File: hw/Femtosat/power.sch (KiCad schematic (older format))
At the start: 10 parts, among them U0 AP7215-33YG-13

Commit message: Added library for certain components. Symbols and footprints were associated.
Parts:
- C2a1, C2b1, C3a1, C3b1, C4, C5, Cr1, Cr2: footprint Capacitor_SMD:C_0805_2012Metric_Pad1.15x1.40mm_HandSolder -> Capacitor_SMD:C_0603_1608Metric_Pad1.05x0.95mm_HandSolder
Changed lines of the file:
@@
 F 0 "C2b1" H 5165 3696 50  0000 L CNN
 F 1 "100nF" H 5165 3605 50  0000 L CNN
-F 2 "Capacitor_SMD:C_0805_2012Metric_Pad1.15x1.40mm_HandSolder" H 5088 3500 50  0001 C CNN
+F 2 "Capacitor_SMD:C_0603_1608Metric_Pad1.05x0.95mm_HandSolder" H 5088 3500 50  0001 C CNN
 F 3 "~" H 5050 3650 50  0001 C CNN
 	1    5050 3650
@@
 F 0 "C5" H 5215 4846 50  0000 L CNN
 F 1 "1uF" H 5215 4755 50  0000 L CNN
-F 2 "Capacitor_SMD:C_0805_2012Metric_Pad1.15x1.40mm_HandSolder" H 5138 4650 50  0001 C CNN
+F 2 "Capacitor_SMD:C_0603_1608Metric_Pad1.05x0.95mm_HandSolder" H 5138 4650 50  0001 C CNN
 F 3 "~" H 5100 4800 50  0001 C CNN
 	1    5100 4800
@@
 F 0 "C2a1" H 4715 3696 50  0000 L CNN
 F 1 "10uF" H 4715 3605 50  0000 L CNN
-F 2 "Capacitor_SMD:C_0805_2012Metric_Pad1.15x1.40mm_HandSolder" H 4638 3500 50  0001 C CNN
+F 2 "Capacitor_SMD:C_0603_1608Metric_Pad1.05x0.95mm_HandSolder" H 4638 3500 50  0001 C CNN
 F 3 "~" H 4600 3650 50  0001 C CNN
 	1    4600 3650
@@
 F 0 "C4" H 4265 4846 50  0000 L CNN
 F 1 "10uF" H 4265 4755 50  0000 L CNN
-F 2 "Capacitor_SMD:C_0805_2012Metric_Pad1.15x1.40mm_HandSolder" H 4188 4650 50  0001 C CNN
+F 2 "Capacitor_SMD:C_0603_1608Metric_Pad1.05x0.95mm_HandSolder" H 4188 4650 50  0001 C CNN
 F 3 "~" H 4150 4800 50  0001 C CNN
 	1    4150 4800
@@
 F 0 "C3a1" H 4715 4296 50  0000 L CNN
 F 1 "100nF" H 4715 4205 50  0000 L CNN
-F 2 "Capacitor_SMD:C_0805_2012Metric_Pad1.15x1.40mm_HandSolder" H 4638 4100 50  0001 C CNN
+F 2 "Capacitor_SMD:C_0603_1608Metric_Pad1.05x0.95mm_HandSolder" H 4638 4100 50  0001 C CNN
 F 3 "~" H 4600 4250 50  0001 C CNN
 	1    4600 4250
@@
 F 0 "C3b1" H 5165 4296 50  0000 L CNN
 F 1 "100nF" H 5165 4205 50  0000 L CNN
-F 2 "Capacitor_SMD:C_0805_2012Metric_Pad1.15x1.40mm_HandSolder" H 5088 4100 50  0001 C CNN
+F 2 "Capacitor_SMD:C_0603_1608Metric_Pad1.05x0.95mm_HandSolder" H 5088 4100 50  0001 C CNN
 F 3 "~" H 5050 4250 50  0001 C CNN
 	1    5050 4250
@@
 F 0 "Cr1" H 3115 3646 50  0000 L CNN
 F 1 "1uF" H 3115 3555 50  0000 L CNN
-F 2 "Capacitor_SMD:C_0805_2012Metric_Pad1.15x1.40mm_HandSolder" H 3038 3450 50  0001 C CNN
+F 2 "Capacitor_SMD:C_0603_1608Metric_Pad1.05x0.95mm_HandSolder" H 3038 3450 50  0001 C CNN
 F 3 "~" H 3000 3600 50  0001 C CNN
 	1    3000 3600
@@
 F 0 "Cr2" H 4115 3646 50  0000 L CNN
 F 1 "1uF" H 4115 3555 50  0000 L CNN
-F 2 "Capacitor_SMD:C_0805_2012Metric_Pad1.15x1.40mm_HandSolder" H 4038 3450 50  0001 C CNN
+F 2 "Capacitor_SMD:C_0603_1608Metric_Pad1.05x0.95mm_HandSolder" H 4038 3450 50  0001 C CNN
 F 3 "~" H 4000 3600 50  0001 C CNN
 	1    4000 3600

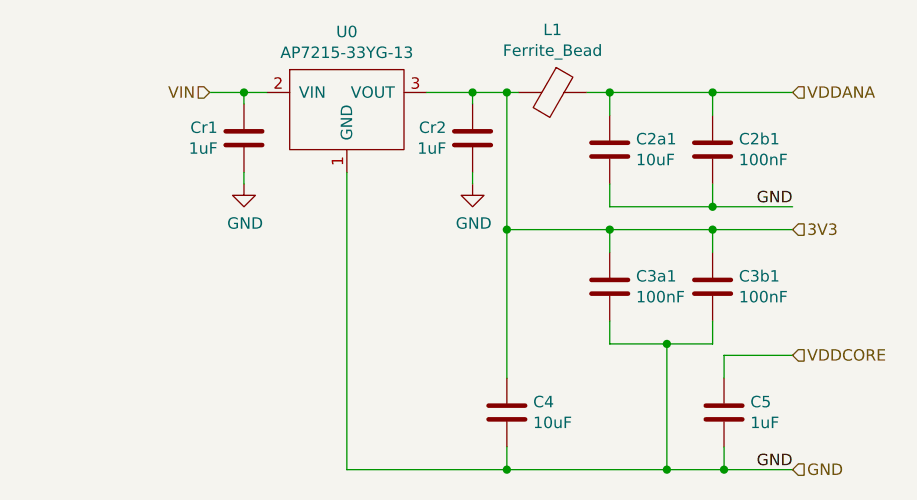
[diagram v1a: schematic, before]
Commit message: Deleted the GPS device (moved to another PCB). Added the deploy-sensor (an interrupter). Moved the programmer to its own hierarchical sheet.
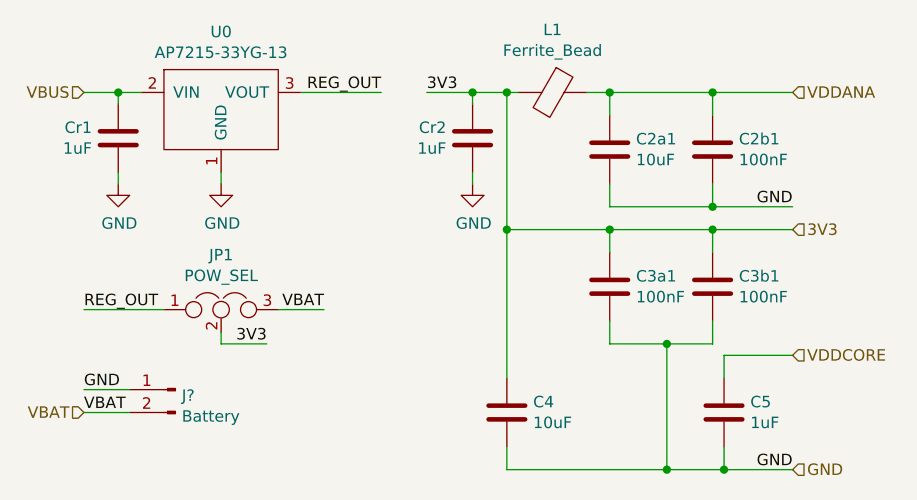
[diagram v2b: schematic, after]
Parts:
- added J?: Battery, symbol Connector:Conn_01x02_Male
- added JP1: POW_SEL, symbol Device:Jumper_NC_Dual
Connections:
- net 3V3: now also JP1.2; no longer U0.3 (VOUT)
- net GND: now also J?.1 (Pin_1)
- net VIN renamed VBUS
- new net REG_OUT: JP1.1, U0.3 (VOUT)
- new net VBAT: J?.2 (Pin_2), JP1.3
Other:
- moved on the sheet: Cr1, U0
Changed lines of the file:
@@
 $Descr A4 11693 8268
 encoding utf-8
-Sheet 2 4
+Sheet 2 5
 Title ""
 Date ""
@@
 L power_regul:AP7215-33YG-13 U0
 U 1 1 5BB07412
-P 3450 3550
-F 0 "U0" H 3450 3965 50  0000 C CNN
-F 1 "AP7215-33YG-13" H 3450 3874 50  0000 C CNN
-F 2 "Package_TO_SOT_SMD:SOT-89-3_Handsoldering" H 3450 3550 50  0001 C CNN
-F 3 "" H 3450 3550 50  0001 C CNN
-	1    3450 3550
+P 2900 3550
+F 0 "U0" H 2900 3965 50  0000 C CNN
+F 1 "AP7215-33YG-13" H 2900 3874 50  0000 C CNN
+F 2 "Package_TO_SOT_SMD:SOT-89-3_Handsoldering" H 2900 3550 50  0001 C CNN
+F 3 "" H 2900 3550 50  0001 C CNN
+	1    2900 3550
 	1    0    0    -1
 $EndComp
@@
 	5400 4000 5050 4000
 Connection ~ 5050 4000
-Connection ~ 4150 5050
-Text HLabel 2850 3400 0    50   Input ~ 0
-VIN
+Text HLabel 2300 3400 0    50   Input ~ 0
+VBUS
 $Comp
 L Device:C Cr1
 U 1 1 5BB30701
-P 3000 3600
-F 0 "Cr1" H 3115 3646 50  0000 L CNN
-F 1 "1uF" H 3115 3555 50  0000 L CNN
-F 2 "Capacitor_SMD:C_0603_1608Metric_Pad1.05x0.95mm_HandSolder" H 3038 3450 50  0001 C CNN
-F 3 "~" H 3000 3600 50  0001 C CNN
-	1    3000 3600
+P 2450 3600
+F 0 "Cr1" H 2565 3646 50  0000 L CNN
+F 1 "1uF" H 2565 3555 50  0000 L CNN
+F 2 "Capacitor_SMD:C_0603_1608Metric_Pad1.05x0.95mm_HandSolder" H 2488 3450 50  0001 C CNN
+F 3 "~" H 2450 3600 50  0001 C CNN
+	1    2450 3600
 	-1   0    0    -1
 $EndComp
@@
 	4000 3400 4150 3400
 Wire Wire Line
-	2850 3400 3000 3400
-Wire Wire Line
-	3000 3450 3000 3400
-Connection ~ 3000 3400
-Wire Wire Line
-	3000 3400 3100 3400
-Wire Wire Line
-	3000 3750 3000 3800
+	2300 3400 2450 3400
+Wire Wire Line
+	2450 3450 2450 3400
+Connection ~ 2450 3400
+Wire Wire Line
+	2450 3400 2550 3400
+Wire Wire Line
+	2450 3750 2450 3800
 Wire Wire Line
 	4000 3750 4000 3800
@@
 L power:GND #PWR0107
 U 1 1 5BB332C0
-P 3000 3800
-F 0 "#PWR0107" H 3000 3550 50  0001 C CNN
-F 1 "GND" H 3005 3627 50  0000 C CNN
-F 2 "" H 3000 3800 50  0001 C CNN
-F 3 "" H 3000 3800 50  0001 C CNN
-	1    3000 3800
+P 2450 3800
+F 0 "#PWR0107" H 2450 3550 50  0001 C CNN
+F 1 "GND" H 2455 3627 50  0000 C CNN
+F 2 "" H 2450 3800 50  0001 C CNN
+F 3 "" H 2450 3800 50  0001 C CNN
+	1    2450 3800
 	1    0    0    -1
 $EndComp
@@
 	1    0    0    -1
 $EndComp
-Wire Wire Line
-	3450 5050 3450 3750
-Wire Wire Line
-	3450 5050 4150 5050
+$Comp
+L Device:Jumper_NC_Dual JP1
+U 1 1 5BF7CE13
+P 2900 4350
+F 0 "JP1" H 2900 4589 50  0000 C CNN
+F 1 "POW_SEL" H 2900 4498 50  0000 C CNN
+F 2 "" H 2900 4350 50  0001 C CNN
+F 3 "~" H 2900 4350 50  0001 C CNN
+	1    2900 4350
+	1    0    0    -1
+$EndComp
+$Comp
+L power:GND #PWR?
+U 1 1 5BF7FABB
+P 2900 3800
+F 0 "#PWR?" H 2900 3550 50  0001 C CNN
+F 1 "GND" H 2905 3627 50  0000 C CNN
+F 2 "" H 2900 3800 50  0001 C CNN
+F 3 "" H 2900 3800 50  0001 C CNN
+	1    2900 3800
+	1    0    0    -1
+$EndComp
+Wire Wire Line
+	2900 3800 2900 3750
+Text Label 3600 3400 2    50   ~ 0
+REG_OUT
+Wire Wire Line
+	3250 3400 3600 3400
+Wire Wire Line
+	2900 4450 2900 4500
+Wire Wire Line
+	2900 4500 3100 4500
+Text Label 3100 4500 2    50   ~ 0
+3V3
+Text Label 2300 4350 0    50   ~ 0
+REG_OUT
+Wire Wire Line
+	2300 4350 2650 4350
+Wire Wire Line
+	3150 4350 3350 4350
+Text Label 3350 4350 2    50   ~ 0
+VBAT
+Text Label 3800 3400 0    50   ~ 0
+3V3
+Text HLabel 2300 4800 0    50   Input ~ 0
+VBAT
+$Comp
+L Connector:Conn_01x02_Male J?
+U 1 1 5BFD4B3E
+P 2700 4700
+F 0 "J?" H 2672 4674 50  0000 R CNN
+F 1 "Battery" H 2672 4583 50  0000 R CNN
+F 2 "" H 2700 4700 50  0001 C CNN
+F 3 "~" H 2700 4700 50  0001 C CNN
+	1    2700 4700
+	-1   0    0    -1
+$EndComp
+Text Label 2300 4700 0    50   ~ 0
+GND
+Text Label 2300 4800 0    50   ~ 0
+VBAT
+Wire Wire Line
+	2500 4700 2300 4700
+Wire Wire Line
+	2300 4800 2500 4800
 $EndSCHEMATC

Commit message: Associated the new symbols to their respective footprints.
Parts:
- J4: renamed from J?; footprint (none) -> Connector_JST:JST_PH_S2B-PH-K_1x02_P2.00mm_Horizontal
- JP1: footprint (none) -> Connector_PinHeader_2.54mm:PinHeader_1x03_P2.54mm_Vertical
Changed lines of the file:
@@
 F 0 "JP1" H 2900 4589 50  0000 C CNN
 F 1 "POW_SEL" H 2900 4498 50  0000 C CNN
-F 2 "" H 2900 4350 50  0001 C CNN
+F 2 "Connector_PinHeader_2.54mm:PinHeader_1x03_P2.54mm_Vertical" H 2900 4350 50  0001 C CNN
 F 3 "~" H 2900 4350 50  0001 C CNN
 	1    2900 4350
@@
 $EndComp
 $Comp
-L power:GND #PWR?
+L power:GND #PWR0113
 U 1 1 5BF7FABB
 P 2900 3800
-F 0 "#PWR?" H 2900 3550 50  0001 C CNN
+F 0 "#PWR0113" H 2900 3550 50  0001 C CNN
 F 1 "GND" H 2905 3627 50  0000 C CNN
 F 2 "" H 2900 3800 50  0001 C CNN
@@
 VBAT
 $Comp
-L Connector:Conn_01x02_Male J?
+L Connector:Conn_01x02_Male J4
 U 1 1 5BFD4B3E
 P 2700 4700
-F 0 "J?" H 2672 4674 50  0000 R CNN
+F 0 "J4" H 2672 4674 50  0000 R CNN
 F 1 "Battery" H 2672 4583 50  0000 R CNN
-F 2 "" H 2700 4700 50  0001 C CNN
+F 2 "Connector_JST:JST_PH_S2B-PH-K_1x02_P2.00mm_Horizontal" H 2700 4700 50  0001 C CNN
 F 3 "~" H 2700 4700 50  0001 C CNN
 	1    2700 4700

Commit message: Minor changes.
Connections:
- net 3V3: no longer Cr2.1
- net GND: now also J4.2 (Pin_2); no longer J4.1 (Pin_1)
- net REG_OUT: now also Cr2.1
- net VBAT: now also J4.1 (Pin_1); no longer J4.2 (Pin_2)
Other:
- moved on the sheet: Cr2
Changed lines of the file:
@@
 L Device:C Cr2
 U 1 1 5BB3073D
-P 4000 3600
-F 0 "Cr2" H 4115 3646 50  0000 L CNN
-F 1 "1uF" H 4115 3555 50  0000 L CNN
-F 2 "Capacitor_SMD:C_0603_1608Metric_Pad1.05x0.95mm_HandSolder" H 4038 3450 50  0001 C CNN
-F 3 "~" H 4000 3600 50  0001 C CNN
-	1    4000 3600
+P 3600 3600
+F 0 "Cr2" H 3715 3646 50  0000 L CNN
+F 1 "1uF" H 3715 3555 50  0000 L CNN
+F 2 "Capacitor_SMD:C_0603_1608Metric_Pad1.05x0.95mm_HandSolder" H 3638 3450 50  0001 C CNN
+F 3 "~" H 3600 3600 50  0001 C CNN
+	1    3600 3600
 	-1   0    0    -1
 $EndComp
-Wire Wire Line
-	3800 3400 4000 3400
 Connection ~ 4150 3400
-Wire Wire Line
-	4000 3450 4000 3400
-Connection ~ 4000 3400
-Wire Wire Line
-	4000 3400 4150 3400
 Wire Wire Line
 	2300 3400 2450 3400
@@
 	2450 3750 2450 3800
 Wire Wire Line
-	4000 3750 4000 3800
+	3600 3750 3600 3800
 $Comp
 L power:GND #PWR0107
@@
 L power:GND #PWR0108
 U 1 1 5BB332E6
-P 4000 3800
-F 0 "#PWR0108" H 4000 3550 50  0001 C CNN
-F 1 "GND" H 4005 3627 50  0000 C CNN
-F 2 "" H 4000 3800 50  0001 C CNN
-F 3 "" H 4000 3800 50  0001 C CNN
-	1    4000 3800
+P 3600 3800
+F 0 "#PWR0108" H 3600 3550 50  0001 C CNN
+F 1 "GND" H 3605 3627 50  0000 C CNN
+F 2 "" H 3600 3800 50  0001 C CNN
+F 3 "" H 3600 3800 50  0001 C CNN
+	1    3600 3800
 	1    0    0    -1
 $EndComp
@@
 Text Label 3800 3400 0    50   ~ 0
 3V3
-Text HLabel 2300 4800 0    50   Input ~ 0
+Text HLabel 2300 4700 0    50   Input ~ 0
 VBAT
 $Comp
@@
 	-1   0    0    -1
 $EndComp
+Text Label 2300 4800 0    50   ~ 0
+GND
 Text Label 2300 4700 0    50   ~ 0
-GND
-Text Label 2300 4800 0    50   ~ 0
 VBAT
 Wire Wire Line
@@
 Wire Wire Line
 	2300 4800 2500 4800
+Wire Wire Line
+	3800 3400 4150 3400
+Wire Wire Line
+	3600 3450 3600 3400
 $EndSCHEMATC

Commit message: Routed all tracks.
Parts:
- removed JP1: POW_SEL, Connector_PinHeader_2.54mm:PinHeader_1x03_P2.54mm_Vertical, symbol Device:Jumper_NC_Dual
- added U3: AV4524, Interrupt:AV4524, symbol Interrupter:AV4524
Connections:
- net 3V3: now also U3.1 (COM)
- net VBAT: now also U3.3 (NC)
- net REG_OUT renamed REG_USB
- net REG_USB: now also U3.2 (NO)
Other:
- moved on the sheet: J4
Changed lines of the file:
@@
-$EndComp
-$Comp
-L Device:Jumper_NC_Dual JP1
-U 1 1 5BF7CE13
-P 2900 4350
-F 0 "JP1" H 2900 4589 50  0000 C CNN
-F 1 "POW_SEL" H 2900 4498 50  0000 C CNN
-F 2 "Connector_PinHeader_2.54mm:PinHeader_1x03_P2.54mm_Vertical" H 2900 4350 50  0001 C CNN
-F 3 "~" H 2900 4350 50  0001 C CNN
-	1    2900 4350
-	1    0    0    -1
 $EndComp
 $Comp
@@
 	2900 3800 2900 3750
 Text Label 3600 3400 2    50   ~ 0
-REG_OUT
+REG_USB
 Wire Wire Line
 	3250 3400 3600 3400
-Wire Wire Line
-	2900 4450 2900 4500
-Wire Wire Line
-	2900 4500 3100 4500
-Text Label 3100 4500 2    50   ~ 0
-3V3
-Text Label 2300 4350 0    50   ~ 0
-REG_OUT
-Wire Wire Line
-	2300 4350 2650 4350
-Wire Wire Line
-	3150 4350 3350 4350
-Text Label 3350 4350 2    50   ~ 0
-VBAT
 Text Label 3800 3400 0    50   ~ 0
 3V3
-Text HLabel 2300 4700 0    50   Input ~ 0
+Text HLabel 2600 4300 0    50   Input ~ 0
 VBAT
 $Comp
 L Connector:Conn_01x02_Male J4
 U 1 1 5BFD4B3E
-P 2700 4700
-F 0 "J4" H 2672 4674 50  0000 R CNN
-F 1 "Battery" H 2672 4583 50  0000 R CNN
-F 2 "Connector_JST:JST_PH_S2B-PH-K_1x02_P2.00mm_Horizontal" H 2700 4700 50  0001 C CNN
-F 3 "~" H 2700 4700 50  0001 C CNN
-	1    2700 4700
+P 3000 4300
+F 0 "J4" H 2972 4274 50  0000 R CNN
+F 1 "Battery" H 2972 4183 50  0000 R CNN
+F 2 "Connector_JST:JST_PH_S2B-PH-K_1x02_P2.00mm_Horizontal" H 3000 4300 50  0001 C CNN
+F 3 "~" H 3000 4300 50  0001 C CNN
+	1    3000 4300
 	-1   0    0    -1
 $EndComp
-Text Label 2300 4800 0    50   ~ 0
+Text Label 2600 4400 0    50   ~ 0
 GND
-Text Label 2300 4700 0    50   ~ 0
+Text Label 2600 4300 0    50   ~ 0
 VBAT
 Wire Wire Line
-	2500 4700 2300 4700
+	2800 4300 2600 4300
 Wire Wire Line
-	2300 4800 2500 4800
+	2600 4400 2800 4400
 Wire Wire Line
 	3800 3400 4150 3400
 Wire Wire Line
 	3600 3450 3600 3400
+$Comp
+L Interrupter:AV4524 U3
+U 1 1 5BFC5BF6
+P 2900 4800
+F 0 "U3" H 3178 4846 50  0000 L CNN
+F 1 "AV4524" H 3178 4755 50  0000 L CNN
+F 2 "Interrupt:AV4524" H 2850 4800 50  0001 C CNN
+F 3 "" H 2850 4800 50  0001 C CNN
+	1    2900 4800
+	-1   0    0    -1
+$EndComp
+Text Label 3450 4700 2    50   ~ 0
+3V3
+Text Label 3450 4900 2    50   ~ 0
+VBAT
+Text Label 3450 4800 2    50   ~ 0
+REG_USB
+Wire Wire Line
+	3450 4800 3100 4800
+Wire Wire Line
+	3100 4900 3450 4900
+Wire Wire Line
+	3100 4700 3450 4700
 $EndSCHEMATC
